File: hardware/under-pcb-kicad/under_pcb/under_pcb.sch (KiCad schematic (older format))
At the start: 7 parts, among them J1 Conn_01x08, J2 Conn_01x08, J3 Conn_01x08, J4 Conn_01x06, J5 Conn_02x18_Odd_Even, J6 Conn_01x08, J7 Conn_01x04

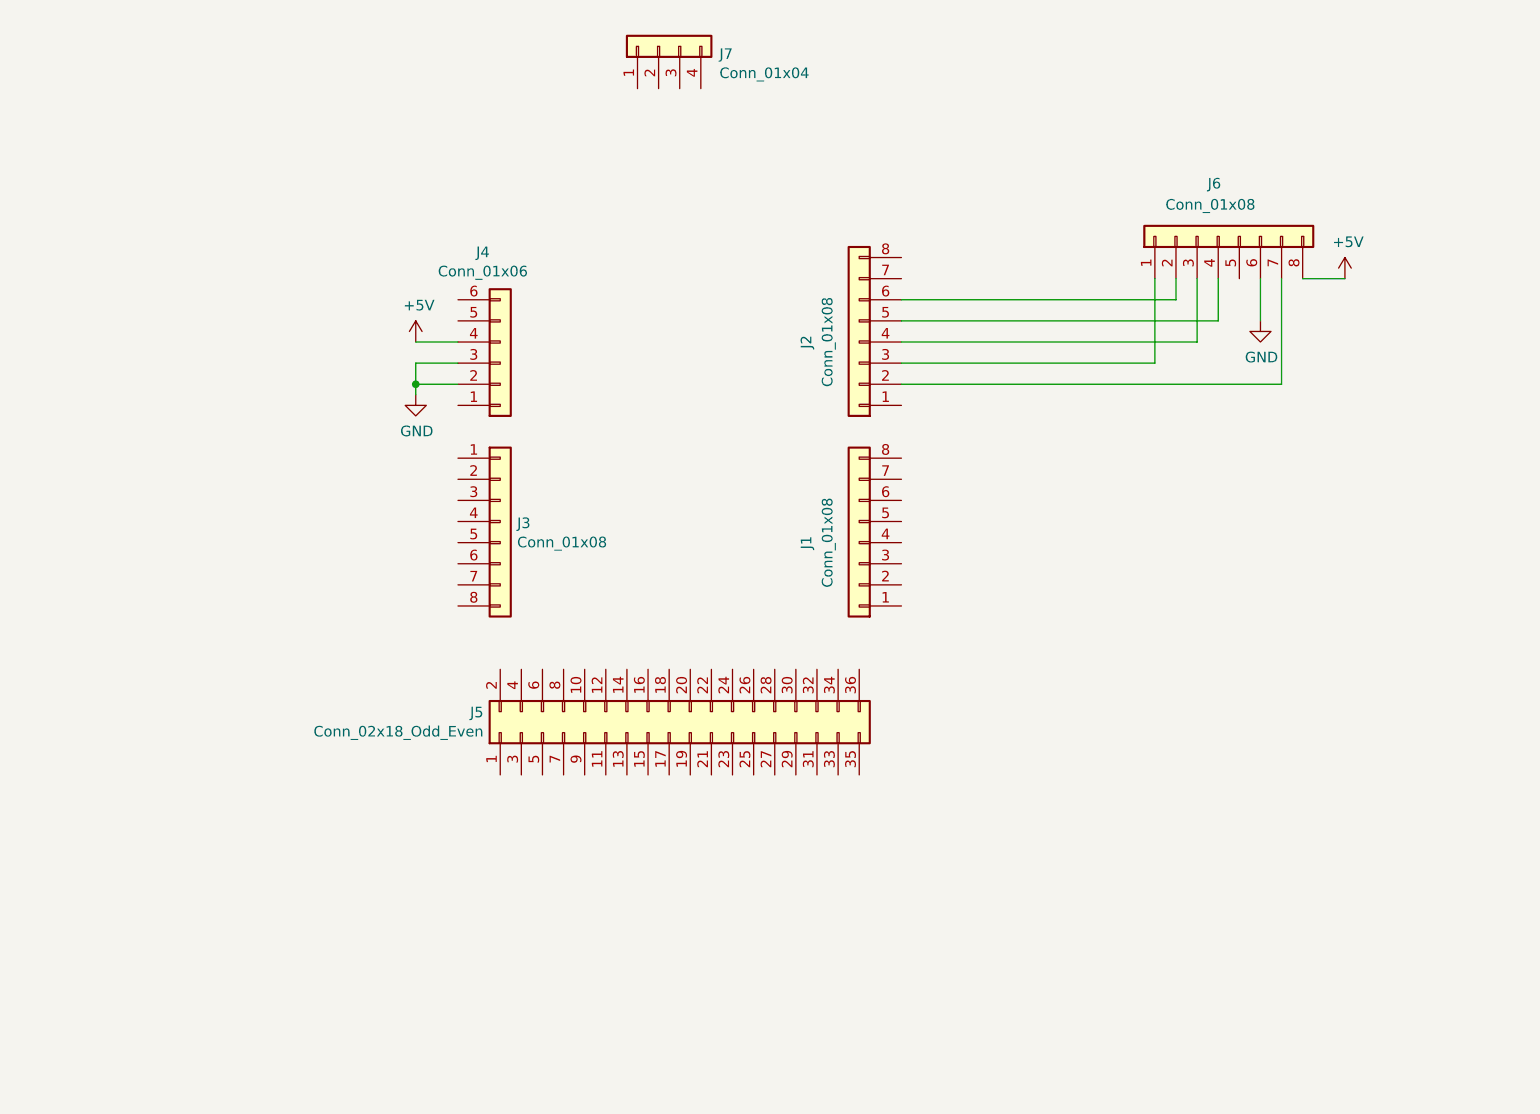
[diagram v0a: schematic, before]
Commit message: wiring and routing under pcb
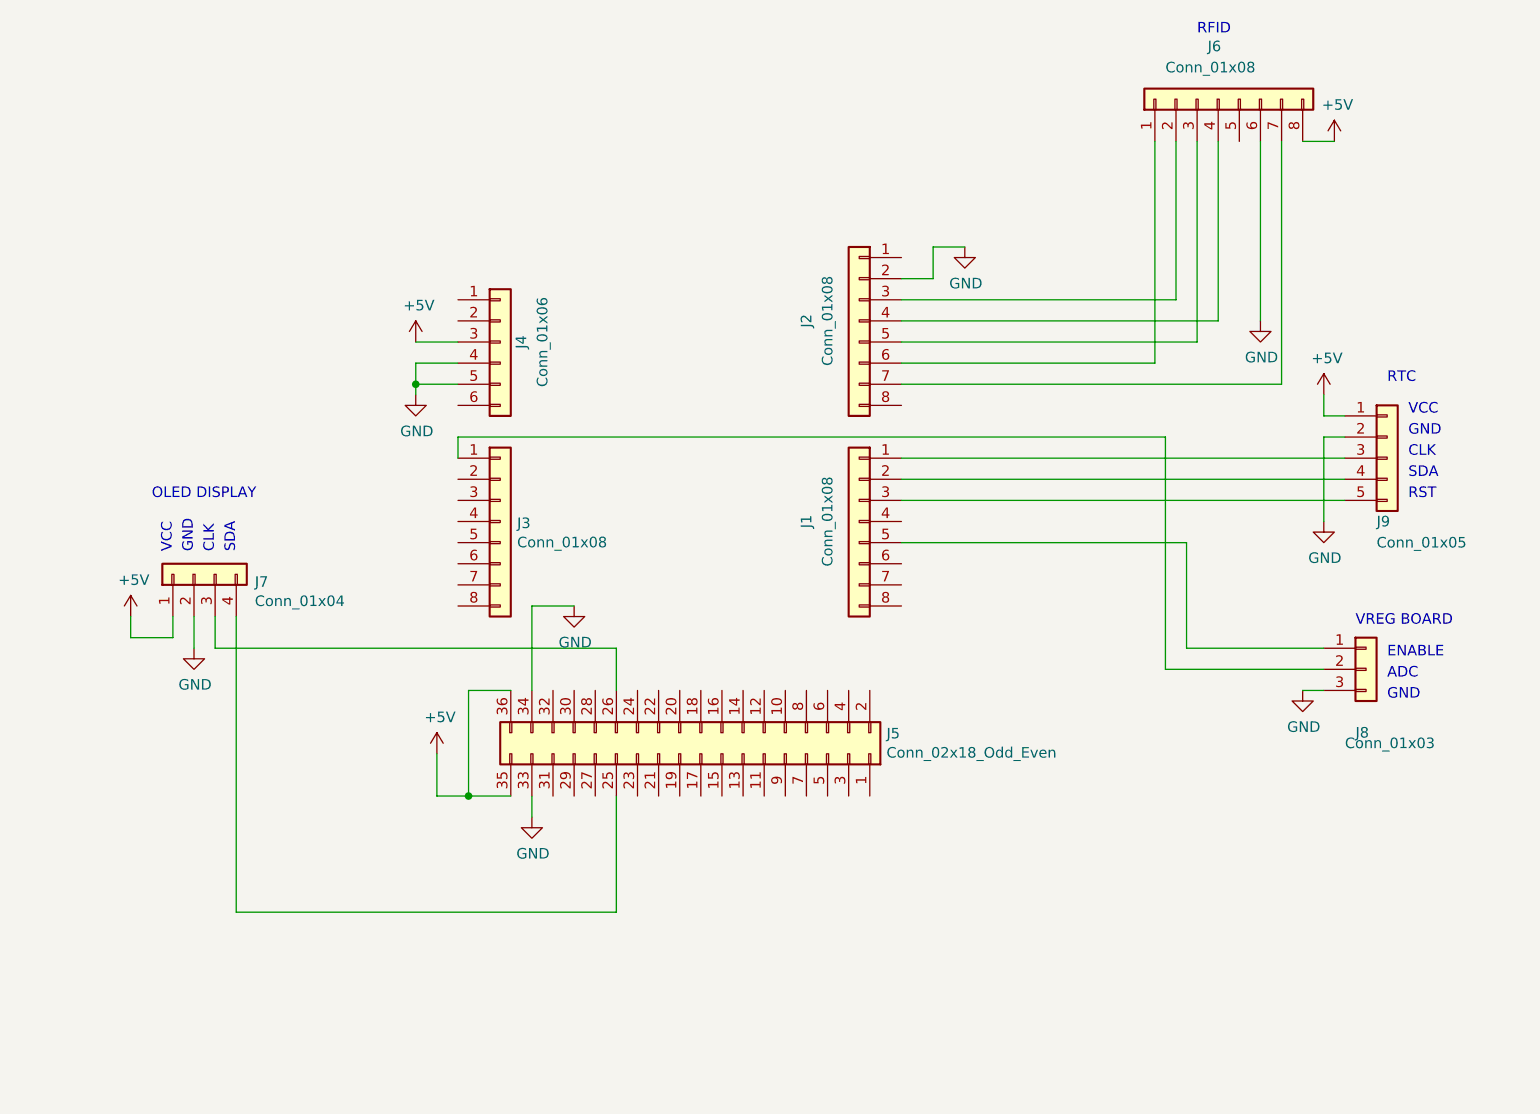
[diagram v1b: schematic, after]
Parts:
- added J8: Conn_01x03, Connector_PinSocket_2.54mm:PinSocket_1x03_P2.54mm_Vertical, symbol Connector_Generic:Conn_01x03
- added J9: Conn_01x05, Connector_PinSocket_2.54mm:PinSocket_1x05_P2.54mm_Vertical, symbol Connector_Generic:Conn_01x05
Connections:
- net +5V: now also J4.3 (Pin_3), J5.35 (Pin_35), J5.36 (Pin_36), J7.1 (Pin_1), J9.1 (Pin_1); no longer J4.4 (Pin_4)
- net GND: now also J2.2 (Pin_2), J4.4 (Pin_4), J4.5 (Pin_5), J5.33 (Pin_33), J5.34 (Pin_34), J7.2 (Pin_2), J8.3 (Pin_3), J9.2 (Pin_2); no longer J4.2 (Pin_2), J4.3 (Pin_3)
- net at J5.25 (Pin_25): now also J7.4 (Pin_4)
- net at J5.26 (Pin_26): now also J7.3 (Pin_3)
- net at J1.1 (Pin_1): now also J9.3 (Pin_3)
- net at J1.2 (Pin_2): now also J9.4 (Pin_4)
- net at J1.3 (Pin_3): now also J9.5 (Pin_5)
- net at J1.5 (Pin_5): now also J8.1 (Pin_1)
- net at J6.7 (Pin_7): now also J2.7 (Pin_7); no longer J2.2 (Pin_2)
- net at J2.3 (Pin_3): now also J6.2 (Pin_2); no longer J6.1 (Pin_1)
- net at J2.4 (Pin_4): now also J6.4 (Pin_4); no longer J6.3 (Pin_3)
- net at J2.5 (Pin_5): now also J6.3 (Pin_3); no longer J6.4 (Pin_4)
- net at J2.6 (Pin_6): now also J6.1 (Pin_1); no longer J6.2 (Pin_2)
- net at J3.1 (Pin_1): now also J8.2 (Pin_2)
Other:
- note added: "ADC"
- note added: "CLK"
- note added: "ENABLE"
- note added: "GND"
- note added: "OLED DISPLAY"
- note added: "RFID"
- note added: "RST"
- note added: "RTC"
- note added: "SDA"
- note added: "VCC"
- note added: "VREG BOARD"
- moved on the sheet: J5, J6, J7

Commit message: board routing donr on under_pcb/patty board
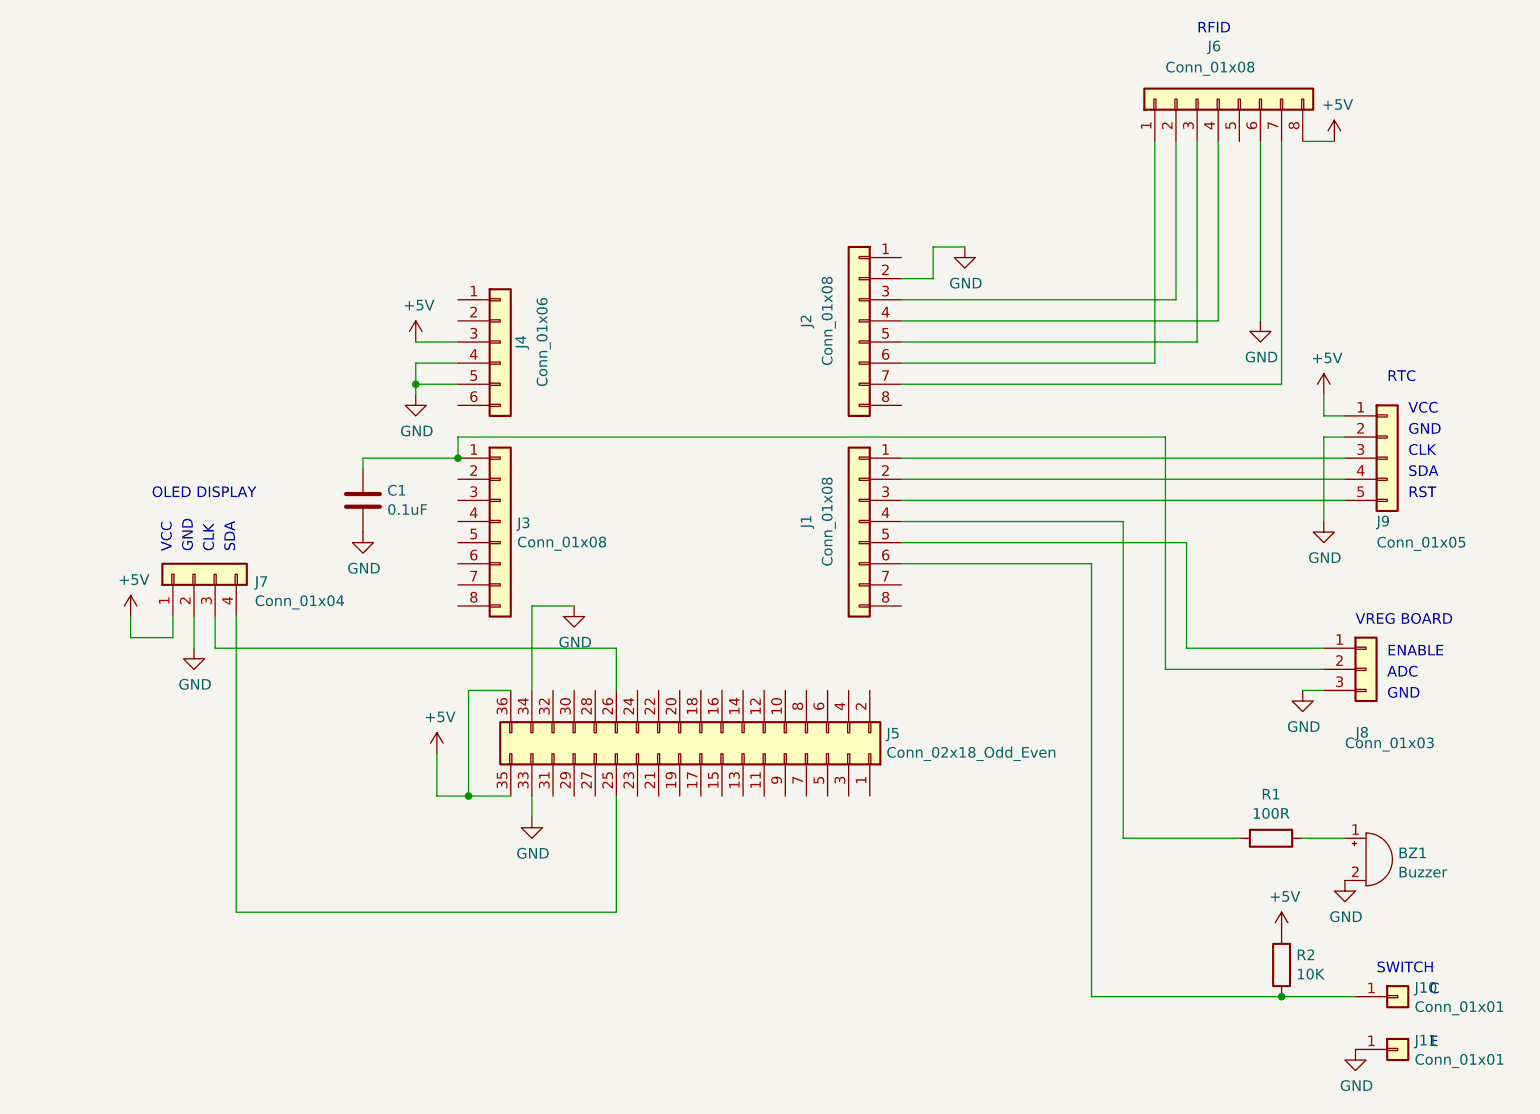
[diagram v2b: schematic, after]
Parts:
- added BZ1: Buzzer, Buzzer_Beeper:Buzzer_12x9.5RM7.6, symbol Device:Buzzer
- added C1: 0.1uF, Capacitor_THT:C_Disc_D5.0mm_W2.5mm_P2.50mm, symbol Device:C
- added J10, J11: Conn_01x01, Connector_PinSocket_2.54mm:PinSocket_1x01_P2.54mm_Vertical, symbol Connector_Generic:Conn_01x01
- added R1: 100R, Resistor_THT:R_Axial_DIN0207_L6.3mm_D2.5mm_P10.16mm_Horizontal, symbol Device:R
- added R2: 10K, Resistor_THT:R_Axial_DIN0207_L6.3mm_D2.5mm_P10.16mm_Horizontal, symbol Device:R
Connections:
- net +5V: now also R2.2
- net GND: now also BZ1.2 (+), C1.2, J11.1 (Pin_1)
- net at J1.4 (Pin_4): now also R1.2
- net at J1.6 (Pin_6): now also J10.1 (Pin_1), R2.1
- net at J3.1 (Pin_1), J8.2 (Pin_2): now also C1.1
- new net: BZ1.1 (-), R1.1
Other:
- note added: "C"
- note added: "E"
- note added: "SWITCH"
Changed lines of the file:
@@
 	7500 3100 7500 2050
 $Comp
-L power:GND #PWR?
+L power:GND #PWR0109
 U 1 1 5E50711A
 P 2950 4450
-F 0 "#PWR?" H 2950 4200 50  0001 C CNN
+F 0 "#PWR0109" H 2950 4200 50  0001 C CNN
 F 1 "GND" H 2955 4277 50  0000 C CNN
 F 2 "" H 2950 4450 50  0001 C CNN
@@
 	4950 5700 4950 5150
 $Comp
-L power:GND #PWR?
+L power:GND #PWR0110
 U 1 1 5E514881
 P 4550 5250
-F 0 "#PWR?" H 4550 5000 50  0001 C CNN
+F 0 "#PWR0110" H 4550 5000 50  0001 C CNN
 F 1 "GND" H 4555 5077 50  0000 C CNN
 F 2 "" H 4550 5250 50  0001 C CNN
@@
 $EndComp
 $Comp
-L power:GND #PWR?
+L power:GND #PWR0111
 U 1 1 5E515CA9
 P 4750 4250
-F 0 "#PWR?" H 4750 4000 50  0001 C CNN
+F 0 "#PWR0111" H 4750 4000 50  0001 C CNN
 F 1 "GND" H 4755 4077 50  0000 C CNN
 F 2 "" H 4750 4250 50  0001 C CNN
@@
 	4550 5250 4550 5150
 $Comp
-L power:+5V #PWR?
+L power:+5V #PWR0112
 U 1 1 5E5183F3
 P 4100 4950
-F 0 "#PWR?" H 4100 4800 50  0001 C CNN
+F 0 "#PWR0112" H 4100 4800 50  0001 C CNN
 F 1 "+5V" H 4115 5123 50  0000 C CNN
 F 2 "" H 4100 4950 50  0001 C CNN
@@
 SDA
 $Comp
-L power:GND #PWR?
+L power:GND #PWR0113
 U 1 1 5E51BD7E
 P 6600 2550
-F 0 "#PWR?" H 6600 2300 50  0001 C CNN
+F 0 "#PWR0113" H 6600 2300 50  0001 C CNN
 F 1 "GND" H 6605 2377 50  0000 C CNN
 F 2 "" H 6600 2550 50  0001 C CNN
@@
 Wire Wire Line
 	6450 2550 6600 2550
+$Comp
+L Device:Buzzer BZ1
+U 1 1 5E4D82B0
+P 8500 5450
+F 0 "BZ1" H 8652 5479 50  0000 L CNN
+F 1 "Buzzer" H 8652 5388 50  0000 L CNN
+F 2 "Buzzer_Beeper:Buzzer_12x9.5RM7.6" V 8475 5550 50  0001 C CNN
+F 3 "~" V 8475 5550 50  0001 C CNN
+	1    8500 5450
+	1    0    0    -1
+$EndComp
+$Comp
+L power:GND #PWR0114
+U 1 1 5E4D9265
+P 8400 5550
+F 0 "#PWR0114" H 8400 5300 50  0001 C CNN
+F 1 "GND" H 8405 5377 50  0000 C CNN
+F 2 "" H 8400 5550 50  0001 C CNN
+F 3 "" H 8400 5550 50  0001 C CNN
+	1    8400 5550
+	1    0    0    -1
+$EndComp
+$Comp
+L Device:R R1
+U 1 1 5E4DAEDF
+P 8050 5350
+F 0 "R1" V 7843 5350 50  0000 C CNN
+F 1 "100R" V 7934 5350 50  0000 C CNN
+F 2 "Resistor_THT:R_Axial_DIN0207_L6.3mm_D2.5mm_P10.16mm_Horizontal" V 7980 5350 50  0001 C CNN
+F 3 "~" H 8050 5350 50  0001 C CNN
+	1    8050 5350
+	0    1    1    0
+$EndComp
+Wire Wire Line
+	8400 5350 8200 5350
+Wire Wire Line
+	6300 3850 7350 3850
+Wire Wire Line
+	7350 3850 7350 5350
+Wire Wire Line
+	7350 5350 7900 5350
+$Comp
+L Device:C C1
+U 1 1 5E4DDF01
+P 3750 3750
+F 0 "C1" H 3865 3796 50  0000 L CNN
+F 1 "0.1uF" H 3865 3705 50  0000 L CNN
+F 2 "Capacitor_THT:C_Disc_D5.0mm_W2.5mm_P2.50mm" H 3788 3600 50  0001 C CNN
+F 3 "~" H 3750 3750 50  0001 C CNN
+	1    3750 3750
+	1    0    0    -1
+$EndComp
+$Comp
+L power:GND #PWR0115
+U 1 1 5E4DEABD
+P 3750 3900
+F 0 "#PWR0115" H 3750 3650 50  0001 C CNN
+F 1 "GND" H 3755 3727 50  0000 C CNN
+F 2 "" H 3750 3900 50  0001 C CNN
+F 3 "" H 3750 3900 50  0001 C CNN
+	1    3750 3900
+	1    0    0    -1
+$EndComp
+Wire Wire Line
+	4200 3550 3750 3550
+Wire Wire Line
+	3750 3550 3750 3600
+Connection ~ 4200 3550
+Text Notes 8550 6000 0    50   ~ 0
+SWITCH
+$Comp
+L power:GND #PWR0116
+U 1 1 5E4E4FB7
+P 8450 6350
+F 0 "#PWR0116" H 8450 6100 50  0001 C CNN
+F 1 "GND" H 8455 6177 50  0000 C CNN
+F 2 "" H 8450 6350 50  0001 C CNN
+F 3 "" H 8450 6350 50  0001 C CNN
+	1    8450 6350
+	1    0    0    -1
+$EndComp
+$Comp
+L Device:R R2
+U 1 1 5E4E7B4E
+P 8100 5950
+F 0 "R2" H 8030 5904 50  0000 R CNN
+F 1 "10K" H 8030 5995 50  0000 R CNN
+F 2 "Resistor_THT:R_Axial_DIN0207_L6.3mm_D2.5mm_P10.16mm_Horizontal" V 8030 5950 50  0001 C CNN
+F 3 "~" H 8100 5950 50  0001 C CNN
+	1    8100 5950
+	-1   0    0    1
+$EndComp
+$Comp
+L power:+5V #PWR0117
+U 1 1 5E4E81CD
+P 8100 5800
+F 0 "#PWR0117" H 8100 5650 50  0001 C CNN
+F 1 "+5V" H 8115 5973 50  0000 C CNN
+F 2 "" H 8100 5800 50  0001 C CNN
+F 3 "" H 8100 5800 50  0001 C CNN
+	1    8100 5800
+	1    0    0    -1
+$EndComp
+Wire Wire Line
+	8450 6100 8100 6100
+Wire Wire Line
+	8100 6100 7200 6100
+Wire Wire Line
+	7200 6100 7200 4050
+Wire Wire Line
+	7200 4050 6300 4050
+Connection ~ 8100 6100
+Text Notes 8800 6100 0    50   ~ 0
+C
+Text Notes 8800 6350 0    50   ~ 0
+E
+$Comp
+L Connector_Generic:Conn_01x01 J10
+U 1 1 5E4F7869
+P 8650 6100
+F 0 "J10" H 8730 6142 50  0000 L CNN
+F 1 "Conn_01x01" H 8730 6051 50  0000 L CNN
+F 2 "Connector_PinSocket_2.54mm:PinSocket_1x01_P2.54mm_Vertical" H 8650 6100 50  0001 C CNN
+F 3 "~" H 8650 6100 50  0001 C CNN
+	1    8650 6100
+	1    0    0    -1
+$EndComp
+$Comp
+L Connector_Generic:Conn_01x01 J11
+U 1 1 5E4F7D40
+P 8650 6350
+F 0 "J11" H 8730 6392 50  0000 L CNN
+F 1 "Conn_01x01" H 8730 6301 50  0000 L CNN
+F 2 "Connector_PinSocket_2.54mm:PinSocket_1x01_P2.54mm_Vertical" H 8650 6350 50  0001 C CNN
+F 3 "~" H 8650 6350 50  0001 C CNN
+	1    8650 6350
+	1    0    0    -1
+$EndComp
 $EndSCHEMATC
